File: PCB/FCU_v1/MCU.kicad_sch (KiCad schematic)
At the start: 27 parts, among them J3 Conn_01x05_Pin, SW1 SW_SPDT, U11 STM32G473RETx, Y2 16MHz

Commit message: Update FCU_v1 PCB and add new resistors
Reworked net assignments and added new nets in FCU_v1.kicad_pcb. Added and repositioned resistors R23 and R28, and updated footprints and net connections. Also updated several backup files and made minor schematic changes in MCU.kicad_sch and PERIPHERALS.kicad_sch.
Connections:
- net GND: now also C16.1, C41.1
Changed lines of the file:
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@@
+	)
+	(junction
+		(at 40.64 110.49)
+		(diameter 0)
+		(color 0 0 0 0)
 	)
 	(junction
@@
 	)
 	(junction
+		(at 39.37 44.45)
+		(diameter 0)
+		(color 0 0 0 0)
+	)
+	(junction
+		(at 33.02 44.45)
+		(diameter 0)
+		(color 0 0 0 0)
+	)
+	(junction
+		(at 39.37 54.61)
+		(diameter 0)
+		(color 0 0 0 0)
+	)
+	(junction
+		(at 52.07 34.29)
+		(diameter 0)
+		(color 0 0 0 0)
+	)
+	(junction
+		(at 33.02 24.13)
+		(diameter 0)
+		(color 0 0 0 0)
+	)
+	(junction
+		(at 158.75 44.45)
+		(diameter 0)
+		(color 0 0 0 0)
+	)
+	(junction
+		(at 52.07 24.13)
+		(diameter 0)
+		(color 0 0 0 0)
+	)
+	(junction
+		(at 49.53 44.45)
+		(diameter 0)
+		(color 0 0 0 0)
+	)
+	(junction
+		(at 39.37 24.13)
+		(diameter 0)
+		(color 0 0 0 0)
+	)
+	(junction
+		(at 39.37 34.29)
+		(diameter 0)
+		(color 0 0 0 0)
+	)
+	(junction
+		(at 68.58 24.13)
+		(diameter 0)
+		(color 0 0 0 0)
+	)
+	(junction
 		(at 40.64 104.14)
 		(diameter 0)
@@
 	)
 	(junction
-		(at 39.37 44.45)
-		(diameter 0)
-		(color 0 0 0 0)
-	)
-	(junction
-		(at 33.02 44.45)
-		(diameter 0)
-		(color 0 0 0 0)
-	)
-	(junction
-		(at 39.37 54.61)
-		(diameter 0)
-		(color 0 0 0 0)
-	)
-	(junction
-		(at 52.07 34.29)
-		(diameter 0)
-		(color 0 0 0 0)
-	)
-	(junction
-		(at 33.02 24.13)
-		(diameter 0)
-		(color 0 0 0 0)
-	)
-	(junction
-		(at 158.75 44.45)
-		(diameter 0)
-		(color 0 0 0 0)
-	)
-	(junction
-		(at 52.07 24.13)
-		(diameter 0)
-		(color 0 0 0 0)
-	)
-	(junction
-		(at 49.53 44.45)
-		(diameter 0)
-		(color 0 0 0 0)
-	)
-	(junction
-		(at 39.37 24.13)
-		(diameter 0)
-		(color 0 0 0 0)
-	)
-	(junction
-		(at 39.37 34.29)
-		(diameter 0)
-		(color 0 0 0 0)
-	)
-	(junction
-		(at 68.58 24.13)
-		(diameter 0)
-		(color 0 0 0 0)
-	)
-	(junction
 		(at 58.42 24.13)
 		(diameter 0)
@@
 	(wire
 		(pts
+			(xy 40.64 110.49) (xy 40.64 111.76)
+		)
+		(stroke
+			(width 0)
+			(type default)
+		)
+	)
+	(wire
+		(pts
 			(xy 58.42 34.29) (xy 68.58 34.29)
 		)
@@
 	(wire
 		(pts
+			(xy 40.64 110.49) (xy 50.8 110.49)
+		)
+		(stroke
+			(width 0)
+			(type default)
+		)
+	)
+	(wire
+		(pts
 			(xy 52.07 24.13) (xy 58.42 24.13)
 		)
@@
 	(wire
 		(pts
-			(xy 30.48 110.49) (xy 50.8 110.49)
+			(xy 30.48 110.49) (xy 40.64 110.49)
 		)
 		(stroke
@@
 	(wire
 		(pts
-			(xy 40.64 104.14) (xy 40.64 111.76)
-		)
-		(stroke
-			(width 0)
-			(type default)
-		)
-	)
-	(wire
-		(pts
 			(xy 38.1 74.93) (xy 36.83 74.93)
 		)
@@
 		)
 		(stroke
+			(width 0)
+			(type default)
+		)
+	)
+	(wire
+		(pts
+			(xy 40.64 104.14) (xy 40.64 110.49)
+		)
+		(stroke

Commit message: Added next version v2
Added notes for next version with what needs to be improved or completely fixed. Notes in schematic file
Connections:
- net SPI_MOSI: now also R21.1, U11.21 (PA7)
- net SPI_SCK: now also R20.1, U11.19 (PA5)
- net CSB_GYR: now reaches R25.2, U11.23 (PC5)
- net CSB_ACCE: now reaches R24.2, U11.22 (PC4)
- net GNSS_Tx: now reaches R14.2, U11.59 (PB6)
- net GNSS_Rst: now reaches R13.2, U11.58 (PB5)
- net CS_MEM: now reaches R26.2, U11.24 (PB0)
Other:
- moved on the sheet: R26
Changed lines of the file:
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@@
 	(wire
 		(pts
-			(xy 179.07 96.52) (xy 173.99 96.52)
+			(xy 182.88 96.52) (xy 173.99 96.52)
 		)
 		(stroke
@@
 	(wire
 		(pts
-			(xy 187.96 96.52) (xy 186.69 96.52)
+			(xy 191.77 96.52) (xy 190.5 96.52)
 		)
 		(stroke
@@
 		)
 	)
+	(label "SPI_SCK"
+		(at 179.07 66.04 0)
+		(effects
+			(font
+				(size 1.27 1.27)
+			)
+			(justify left bottom)
+		)
+	)
+	(label "CS_MEM"
+		(at 175.26 96.52 0)
+		(effects
+			(font
+				(size 1.27 1.27)
+			)
+			(justify left bottom)
+		)
+	)
+	(label "GNSS_Tx"
+		(at 184.15 111.76 0)
+		(effects
+			(font
+				(size 1.27 1.27)
+			)
+			(justify left bottom)
+		)
+	)
+	(label "CSB_GYR"
+		(at 127 88.9 0)
+		(effects
+			(font
+				(size 1.27 1.27)
+			)
+			(justify left bottom)
+		)
+	)
+	(label "CSB_ACCE"
+		(at 127 86.36 0)
+		(effects
+			(font
+				(size 1.27 1.27)
+			)
+			(justify left bottom)
+		)
+	)
+	(label "GNSS_Rst"
+		(at 184.15 109.22 0)
+		(effects
+			(font
+				(size 1.27 1.27)
+			)
+			(justify left bottom)
+		)
+	)
+	(label "SPI_MOSI"
+		(at 179.07 71.12 0)
+		(effects
+			(font
+				(size 1.27 1.27)
+			)
+			(justify left bottom)
+		)
+	)
 	(global_label "3V3_FCU"
 		(shape input)
@@
 	(global_label "CS_MEMO"
 		(shape input)
-		(at 187.96 96.52 0)
+		(at 191.77 96.52 0)
 		(fields_autoplaced yes)
 		(effects
@@
 		)
 		(property "Intersheetrefs" "${INTERSHEET_REFS}"
-			(at 199.7746 96.52 0)
+			(at 203.5846 96.52 0)
 			(effects
 				(font
@@
 	(symbol
 		(lib_id "Device:R")
-		(at 182.88 96.52 270)
+		(at 186.69 96.52 270)
 		(mirror x)
 		(unit 1)
@@
 		(dnp no)
 		(property "Reference" "R26"
-			(at 178.816 94.488 90)
+			(at 182.626 94.488 90)
 			(effects
 				(font
@@
 		)
 		(property "Value" "33R"
-			(at 183.642 94.488 90)
+			(at 187.452 94.488 90)
 			(effects
 				(font
@@
 		)
 		(property "Footprint" "Resistor_SMD:R_0603_1608Metric"
-			(at 182.88 98.298 90)
+			(at 186.69 98.298 90)
 			(effects
 				(font
@@
 		)
 		(property "Datasheet" "~"
-			(at 182.88 96.52 0)
+			(at 186.69 96.52 0)
 			(effects
 				(font
@@
 		)
 		(property "Description" "Resistor"
-			(at 182.88 96.52 0)
+			(at 186.69 96.52 0)
 			(effects
 				(font

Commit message: Layout update
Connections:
- net GNSS_Rst: no longer U11.58 (PB5)
- net GNSS_Tx: no longer U11.59 (PB6)
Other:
- note added: "PB5 PB6"
- note added: "This is for future version with GPS"
- moved on the sheet: R13, R14
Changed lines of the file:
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@@
 	)
 	(rectangle
+		(start 230.505 13.97)
+		(end 280.035 31.115)
+		(stroke
+			(width 0)
+			(type default)
+		)
+		(fill
+			(type none)
+		)
+	)
+	(rectangle
 		(start 16.51 59.69)
 		(end 52.07 85.09)
@@
 		)
 	)
+	(text "This is for future version with GPS"
+		(exclude_from_sim no)
+		(at 254.508 16.51 0)
+		(effects
+			(font
+				(size 1.27 1.27)
+			)
+		)
+	)
+	(text "PB5\nPB6"
+		(exclude_from_sim no)
+		(at 234.95 23.114 0)
+		(effects
+			(font
+				(size 1.27 1.27)
+			)
+		)
+	)
 	(text "SWD"
 		(exclude_from_sim no)
@@
 	(wire
 		(pts
+			(xy 237.49 21.59) (xy 252.73 21.59)
+		)
+		(stroke
+			(width 0)
+			(type default)
+		)
+	)
+	(wire
+		(pts
 			(xy 45.72 34.29) (xy 45.72 33.02)
 		)
@@
 	(wire
 		(pts
-			(xy 207.01 109.22) (xy 205.74 109.22)
+			(xy 262.89 21.59) (xy 260.35 21.59)
 		)
 		(stroke
@@
 	(wire
 		(pts
-			(xy 173.99 109.22) (xy 198.12 109.22)
-		)
-		(stroke
-			(width 0)
-			(type default)
-		)
-	)
-	(wire
-		(pts
 			(xy 151.13 44.45) (xy 151.13 45.72)
 		)
@@
 	(wire
 		(pts
-			(xy 207.01 111.76) (xy 205.74 111.76)
+			(xy 262.89 24.13) (xy 260.35 24.13)
 		)
 		(stroke
@@
 	(wire
 		(pts
+			(xy 237.49 24.13) (xy 252.73 24.13)
+		)
+		(stroke
+			(width 0)
+			(type default)
+		)
+	)
+	(wire
+		(pts
 			(xy 116.84 96.52) (xy 124.46 96.52)
 		)
@@
 	(wire
 		(pts
-			(xy 173.99 111.76) (xy 198.12 111.76)
-		)
-		(stroke
-			(width 0)
-			(type default)
-		)
-	)
-	(wire
-		(pts
 			(xy 39.37 53.34) (xy 39.37 54.61)
 		)
@@
 	)
 	(label "GNSS_Tx"
-		(at 184.15 111.76 0)
+		(at 240.03 24.13 0)
 		(effects
 			(font
@@
 	)
 	(label "GNSS_Rst"
-		(at 184.15 109.22 0)
+		(at 240.03 21.59 0)
 		(effects
 			(font
@@
 	(global_label "GNSS_RST"
 		(shape input)
-		(at 207.01 109.22 0)
+		(at 262.89 21.59 0)
 		(fields_autoplaced yes)
 		(effects
@@
 		)
 		(property "Intersheetrefs" "${INTERSHEET_REFS}"
-			(at 219.4294 109.22 0)
+			(at 275.3094 21.59 0)
 			(effects
 				(font
@@
 	(global_label "GNSS_TX"
 		(shape input)
-		(at 207.01 111.76 0)
+		(at 262.89 24.13 0)
 		(fields_autoplaced yes)
 		(effects
@@
 		)
 		(property "Intersheetrefs" "${INTERSHEET_REFS}"
-			(at 218.1594 111.76 0)
+			(at 274.0394 24.13 0)
 			(effects
 				(font
@@
 	(symbol
 		(lib_id "Device:R")
-		(at 201.93 111.76 270)
+		(at 256.54 24.13 270)
 		(mirror x)
 		(unit 1)
@@
 		(dnp no)
 		(property "Reference" "R14"
-			(at 206.502 113.792 90)
+			(at 261.112 26.162 90)
 			(effects
 				(font
@@
 		)
 		(property "Value" "33R"
-			(at 201.676 113.792 90)
+			(at 256.286 26.162 90)
 			(effects
 				(font
@@
 		)
 		(property "Footprint" "Resistor_SMD:R_0603_1608Metric"
-			(at 201.93 113.538 90)
+			(at 256.54 25.908 90)
 			(effects
 				(font
@@
 		)
 		(property "Datasheet" "~"
-			(at 201.93 111.76 0)
+			(at 256.54 24.13 0)
 			(effects
 				(font
@@
 		)
 		(property "Description" "Resistor"
-			(at 201.93 111.76 0)
+			(at 256.54 24.13 0)
 			(effects
 				(font
@@
 	(symbol
 		(lib_id "Device:R")
-		(at 201.93 109.22 270)
+		(at 256.54 21.59 270)
 		(mirror x)
 		(unit 1)
@@
 		(dnp no)
 		(property "Reference" "R13"
-			(at 205.74 107.188 90)
+			(at 260.35 19.558 90)
 			(effects
 				(font
@@
 		)
 		(property "Value" "33R"
-			(at 200.914 107.188 90)
+			(at 255.524 19.558 90)
 			(effects
 				(font
@@
 		)
 		(property "Footprint" "Resistor_SMD:R_0603_1608Metric"
-			(at 201.93 110.998 90)
+			(at 256.54 23.368 90)
 			(effects
 				(font
@@
 		)
 		(property "Datasheet" "~"
-			(at 201.93 109.22 0)
+			(at 256.54 21.59 0)
 			(effects
 				(font
@@
 		)
 		(property "Description" "Resistor"
-			(at 201.93 109.22 0)
+			(at 256.54 21.59 0)
 			(effects
 				(font

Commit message: Schematic update
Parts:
- added C31: 100n, Capacitor_SMD:C_0805_2012Metric, symbol Device:C
- added C33: 1uF, Capacitor_SMD:C_0805_2012Metric, symbol Device:C
- added C34: 100nF, Capacitor_SMD:C_0805_2012Metric, symbol Device:C
- added D9: ESD2CAN24DBZRQ1, Package_TO_SOT_SMD:SOT-23-3, symbol Power_Protection:ESDA5V3L
- added R10, R11, R12, R9: DNP, Resistor_SMD:R_0201_0603Metric, symbol Device:R
- added R22: 33R, Resistor_SMD:R_0603_1608Metric, symbol Device:R
- added R32, R33, R49, R50: 22Ω, Resistor_SMD:R_0603_1608Metric, symbol Device:R
- added R51: 120R, Resistor_SMD:R_0603_1608Metric, symbol Device:R
- added U10: SN65HVD232, Package_SO:SOIC-8_3.9x4.9mm_P1.27mm, symbol Interface_CAN_LIN:SN65HVD230
- added U3: W25Q128JVSIM, Package_SO:SOIC-8_5.3x5.3mm_P1.27mm, symbol Memory_Flash:W25Q128JVS
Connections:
- net CAN_RX: now also R33.1
- net CAN_TX: now also R32.1
- net CS_MEMO: now also U3.1 (~{CS})
- net GND: now also C31.2, C33.2, C34.2, D9.3 (A), R10.1, R11.1, U10.2 (GND), U3.4 (GND)
- net I2C_SCL: now also R17.2; no longer R17.1
- net I2C_SDA: now also R18.2; no longer R18.1
- net SPI_MISO: now also R22.1
- net SPI_MOSI: now also U3.5 (DI/IO_{0})
- net SPI_SCK: now also U3.6 (CLK)
- net 3V3_FCU renamed +3.3V
- net +3.3V: now also R17.1, R18.1, C31.1, C33.1, C34.1, R12.2, R9.2, U10.3 (VCC), U3.8 (VCC); no longer R17.2, R18.2
- net STM_VDDA renamed +3.3VA
- new net: R50.1, R51.1, U10.6 (CANL)
- new net: R49.1, R51.2, U10.7 (CANH)
- new net: R11.2, R12.1, U3.7 (~{HOLD}/~{RESET}/IO_{3})
- new net: R10.2, R9.1, U3.3 (~{WP}/IO_{2})
- new net: R33.2, U10.4 (R)
- new net: R32.2, U10.1 (D)
- new net: R22.2, U3.2 (DO/IO_{1})
- new net CAN_H: D9.1 (K), R49.2
- new net CAN_L: D9.2 (K), R50.2
- no-connect marks 0 -> 2
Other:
- note added: "120R at 100 MHz"
- note added: "CAN"
- note added: "Memory"
- moved on the sheet: R13, R14, R17, R18, R20, R21, R24, R25, R26, U11

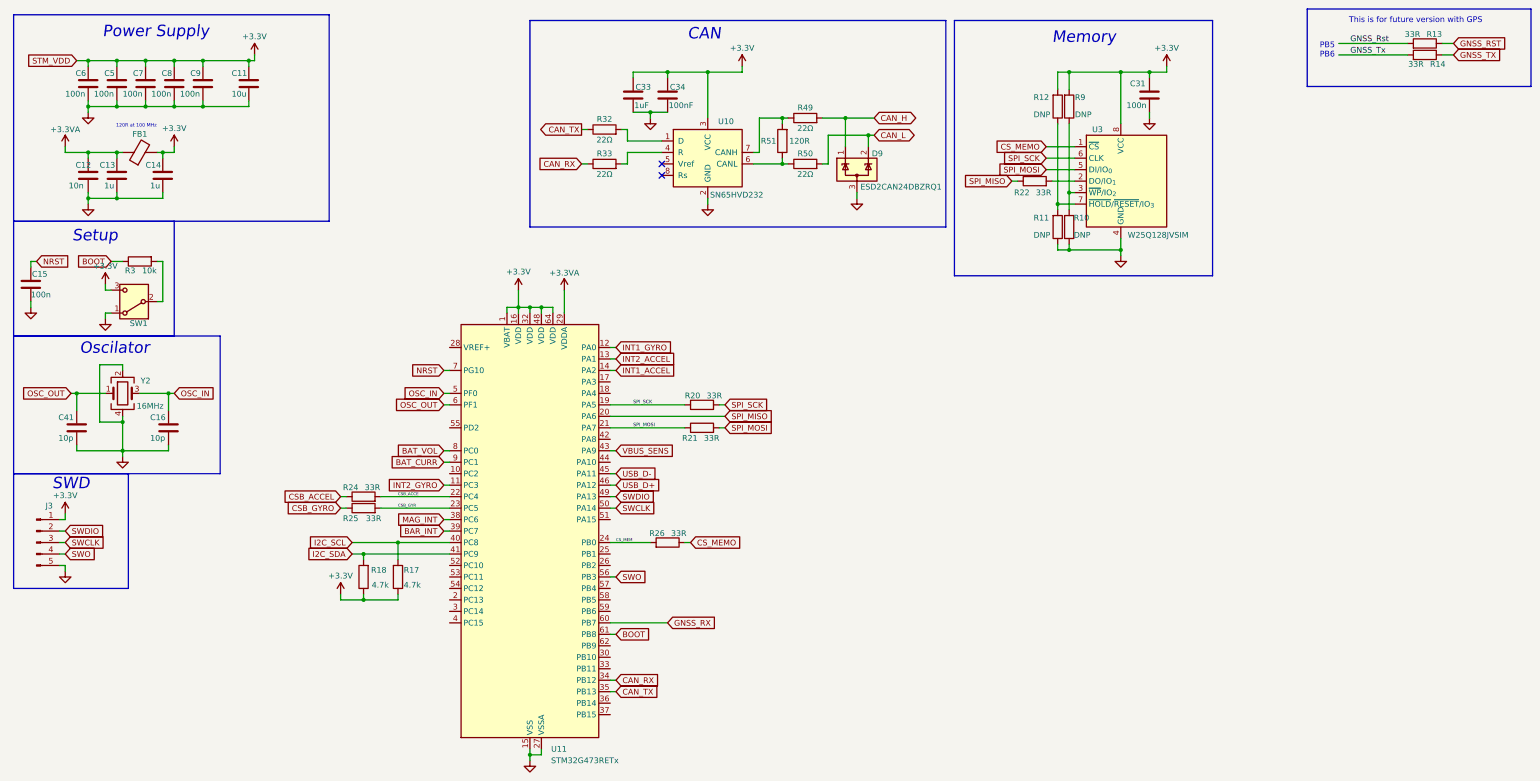
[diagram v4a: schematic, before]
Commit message: Components change and layout update
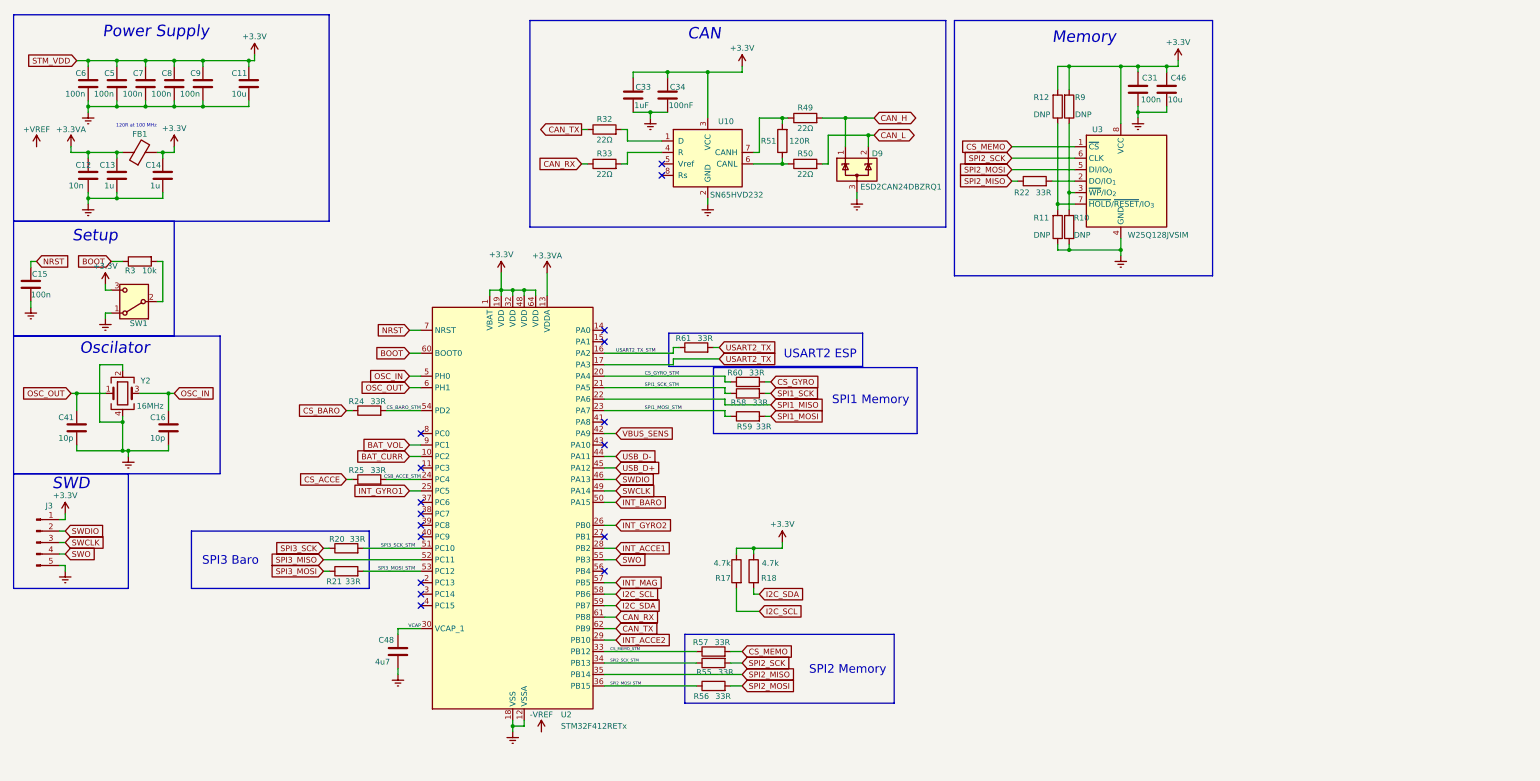
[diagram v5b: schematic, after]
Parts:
- removed R13, R14, R26: 33R, Resistor_SMD:R_0603_1608Metric, symbol Device:R
- removed U11: STM32G473RETx, Package_QFP:LQFP-64_10x10mm_P0.5mm, symbol MCU_ST_STM32G4:STM32G473RETx
- added C46: 10u, Capacitor_SMD:C_0805_2012Metric, symbol Device:C
- added C48: 4u7, Capacitor_SMD:C_0805_2012Metric, symbol Device:C
- added R55, R56, R57, R58, R59, R60, R61: 33R, Resistor_SMD:R_0603_1608Metric, symbol Device:R
- added U2: STM32F412RETx, Package_QFP:LQFP-64_10x10mm_P0.5mm, symbol MCU_ST_STM32F4:STM32F412RETx
- C12, C5, C6, C7, C8, C9: footprint Capacitor_SMD:C_0805_2012Metric -> Capacitor_SMD:C_0603_1608Metric
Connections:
- net +3.3V: now also C46.1, U2.1 (VBAT), U2.19 (VDD), U2.32 (VDD), U2.48 (VDD), U2.64 (VDD)
- net +3.3VA: now also U2.13 (VDDA)
- net BAT_CURR: now also U2.10 (PC2)
- net BAT_VOL: now also U2.9 (PC1)
- net BOOT: now also U2.60 (BOOT0)
- net CAN_RX: now also U2.61 (PB8)
- net CAN_TX: now also U2.62 (PB9)
- net CS_MEMO: now also R57.2
- net GND: now also C46.2, C48.2, U2.12 (VSSA), U2.18 (VSS), U2.31 (VSS), U2.47 (VSS), U2.63 (VSS)
- net I2C_SCL: now also U2.58 (PB6)
- net I2C_SDA: now also U2.59 (PB7)
- net NRST: now also U2.7 (NRST)
- net OSC_IN: now also U2.5 (PH0)
- net OSC_OUT: now also U2.6 (PH1)
- net SWCLK: now also U2.49 (PA14)
- net SWDIO: now also U2.46 (PA13)
- net SWO: now also U2.55 (PB3)
- net USB_D+: now also U2.45 (PA12)
- net USB_D-: now also U2.44 (PA11)
- net VBUS_SENS: now also U2.42 (PA9)
- net CSB_ACCE renamed CS_BARO_STM
- net CS_BARO_STM: now also U2.54 (PD2)
- net CSB_ACCEL renamed CS_BARO
- net CSB_GYR renamed CSB_ACCE_STM
- net CSB_ACCE_STM: now also U2.24 (PC4)
- net CSB_GYRO renamed CS_ACCE
- net SPI_MISO renamed SPI2_MISO
- net SPI2_MISO: now also U2.35 (PB14)
- removed net SPI_MOSI: R21.1, R21.2, U3.5 (DI/IO_{0})
- removed net SPI_SCK: R20.1, R20.2, U3.6 (CLK)
- new net CS_GYRO: R60.2
- new net CS_GYRO_STM: R60.1, U2.20 (PA4)
- new net CS_MEMO_STM: R57.1, U2.33 (PB12)
- new net INT_ACCE1: U2.28 (PB2)
- new net INT_ACCE2: U2.29 (PB10)
- new net INT_BARO: U2.50 (PA15)
- new net INT_GYRO1: U2.25 (PC5)
- new net INT_GYRO2: U2.26 (PB0)
- new net INT_MAG: U2.57 (PB5)
- new net SPI1_MISO: U2.22 (PA6)
- new net SPI1_MOSI: R59.2
- new net SPI1_MOSI_STM: R59.1, U2.23 (PA7)
- new net SPI1_SCK: R58.2
- new net SPI1_SCK_STM: R58.1, U2.21 (PA5)
- new net SPI2_MOSI: R56.2, U3.5 (DI/IO_{0})
- new net SPI2_MOSI_STM: R56.1, U2.36 (PB15)
- new net SPI2_SCK: R55.2, U3.6 (CLK)
- new net SPI2_SCK_STM: R55.1, U2.34 (PB13)
- new net SPI3_MISO: U2.52 (PC11)
- new net SPI3_MOSI: R21.1
- new net SPI3_MOSI_STM: R21.2, U2.53 (PC12)
- new net SPI3_SCK: R20.1
- new net SPI3_SCK_STM: R20.2, U2.51 (PC10)
- new net USART2_TX: R61.2, U2.17 (PA3)
- new net USART2_TX_STM: R61.1, U2.16 (PA2)
- new net VCAP: C48.1, U2.30 (VCAP_1)
- no-connect marks 2 -> 17
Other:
- note added: "SPI1 Memory"
- note added: "SPI2 Memory"
- note added: "SPI3 Baro"
- note added: "USART2 ESP"
- note removed: "PB5 PB6"
- note removed: "This is for future version with GPS"
- moved on the sheet: C31, R17, R18, R20, R21, R24

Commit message: Layout update
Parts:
- removed J3: Conn_01x05_Pin, Connector_PinHeader_2.54mm:PinHeader_1x05_P2.54mm_Vertical, symbol Connector:Conn_01x05_Pin
- removed R49, R50: 22Ω, Resistor_SMD:R_0603_1608Metric, symbol Device:R
- removed SW1: SW_SPDT, symbol Switch:SW_SPDT
- added J12, J13, J3: Conn_01x02_Pin, Connector_PinHeader_2.54mm:PinHeader_1x02_P2.54mm_Vertical, symbol Connector:Conn_01x02_Pin
- added R39, R42: DNP, Resistor_SMD:R_0201_0603Metric, symbol Device:R
- added R41: 10k, Resistor_SMD:R_0603_1608Metric, symbol Device:R
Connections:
- net CAN_H is gone; now on net CAN+: D9.1 (K)
- net CAN_L is gone; now on net CAN-: D9.2 (K)
- net +3.3V: now also J3.1 (Pin_1), R41.1
- net BAT_CURR: now also U2.9 (PC1); no longer U2.10 (PC2)
- net BAT_VOL: now also U2.10 (PC2); no longer U2.9 (PC1)
- net CAN_RX: now also R32.1; no longer R33.1
- net CAN_TX: now also R33.2, U10.1 (D); no longer R32.1, U2.62 (PB9)
- net GND: now also J3.2 (Pin_2), R39.2
- net NRST: now also J12.1 (Pin_1), R42.2
- net SWCLK: now also J13.1 (Pin_1)
- net SWDIO: now also J12.2 (Pin_2)
- net SWO: now also J13.2 (Pin_2)
- net USART2_TX: no longer U2.17 (PA3)
- net at R3.2: now also R39.1
- net CAN-: now reaches R51.1, U10.6 (CANL)
- net CAN+: now reaches R51.2, U10.7 (CANH)
- net at U10.4 (R): now also R32.2; no longer R33.2
- new net: R41.2, R42.1
- new net CAN_TX_STM: R33.1, U2.62 (PB9)
- new net USART2_RX: U2.17 (PA3)
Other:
- moved on the sheet: C15, C16, C41, D9, R3, R32, Y2

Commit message: Layout update
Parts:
- R42: footprint Resistor_SMD:R_0201_0603Metric -> Resistor_SMD:R_0402_1005Metric
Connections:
- net NRST: now also J13.1 (Pin_1); no longer J12.1 (Pin_1)
- net SWCLK: now also J12.2 (Pin_2); no longer J13.1 (Pin_1)
- net SWDIO: now also J13.2 (Pin_2); no longer J12.2 (Pin_2)
- net SWO: now also J12.1 (Pin_1); no longer J13.2 (Pin_2)
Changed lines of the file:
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@@
 	(global_label "SWCLK"
 		(shape input)
-		(at 29.21 137.16 0)
+		(at 29.21 134.62 0)
 		(fields_autoplaced yes)
 		(effects
@@
 		)
 		(property "Intersheetrefs" "${INTERSHEET_REFS}"
-			(at 38.4242 137.16 0)
+			(at 38.4242 134.62 0)
 			(effects
 				(font
@@
 	(global_label "SWDIO"
 		(shape input)
-		(at 29.21 134.62 0)
+		(at 29.21 139.7 0)
 		(fields_autoplaced yes)
 		(effects
@@
 		)
 		(property "Intersheetrefs" "${INTERSHEET_REFS}"
-			(at 38.0614 134.62 0)
+			(at 38.0614 139.7 0)
 			(effects
 				(font
@@
 	(global_label "NRST"
 		(shape output)
-		(at 29.21 132.08 0)
+		(at 29.21 137.16 0)
 		(fields_autoplaced yes)
 		(effects
@@
 		)
 		(property "Intersheetrefs" "${INTERSHEET_REFS}"
-			(at 36.9728 132.08 0)
+			(at 36.9728 137.16 0)
 			(effects
 				(font
@@
 	(global_label "SWO"
 		(shape input)
-		(at 29.21 139.7 0)
+		(at 29.21 132.08 0)
 		(fields_autoplaced yes)
 		(effects
@@
 		)
 		(property "Intersheetrefs" "${INTERSHEET_REFS}"
-			(at 36.1866 139.7 0)
+			(at 36.1866 132.08 0)
 			(effects
 				(font
@@
 			)
 		)
-		(property "Footprint" "Resistor_SMD:R_0201_0603Metric"
+		(property "Footprint" "Resistor_SMD:R_0402_1005Metric"
 			(at 43.18 76.962 90)
 			(effects
